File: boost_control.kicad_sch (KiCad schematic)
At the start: 0 parts

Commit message: Working on 5v supply
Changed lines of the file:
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@@
 	(generator_version "9.0")
 	(paper "A4")
-	(wire
-		(pts
-			(xy 116.84 91.44) (xy 133.35 91.44)
-		)
-		(stroke
-			(width 0)
-			(type default)
-		)
-	)
 	(bus
 		(pts
@@
 		)
 	)
-	(hierarchical_label "FB_OUT"
-		(shape output)
-		(at 133.35 91.44 0)
-		(effects
-			(font
-				(size 1.27 1.27)
-			)
-			(justify left)
-		)
-	)

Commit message: Adding control stuff
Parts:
- added C75: 100nF, Capacitor_SMD:C_0603_1608Metric, symbol Device:C
- added C78: 10uF, Capacitor_SMD:C_0805_2012Metric, symbol Device:C
- added R72: 15k, Resistor_SMD:R_0603_1608Metric, symbol Device:R_US
- added R74: 274k, Resistor_SMD:R_0603_1608Metric, symbol Device:R_US
- added U16: AD5259BRMZ100, RM_10_ADI, symbol _AD5259:AD5259BRMZ100
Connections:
- new net: R72.1, U16.1 (W), U16.10 (A)
- new net: R74.1, U16.9 (B)
- new net +3V3: U16.6 (VLOGIC)
- new net +5V: C75.1, C78.1, U16.8 (VDD)
- new net GND: C75.2, C78.2, U16.7 (GND)
- new net R+: R72.2
- new net R-: R74.2
- new net SCL: U16.5 (SCL)
- new net SDA: U16.4 (SDA)
- no-connect marks 0 -> 2

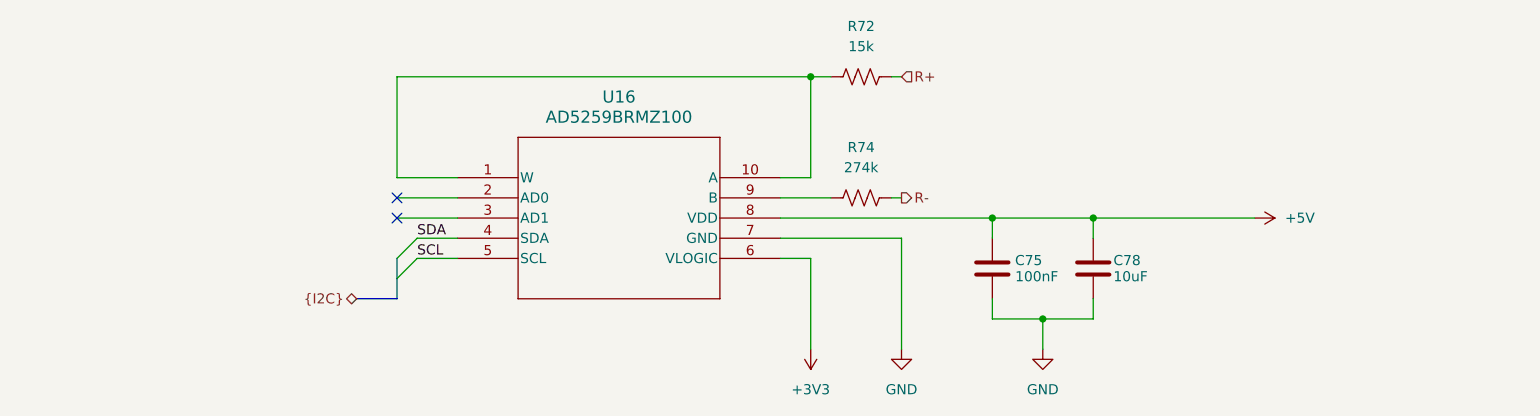
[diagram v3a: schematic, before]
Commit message: Adding in connections to schematic
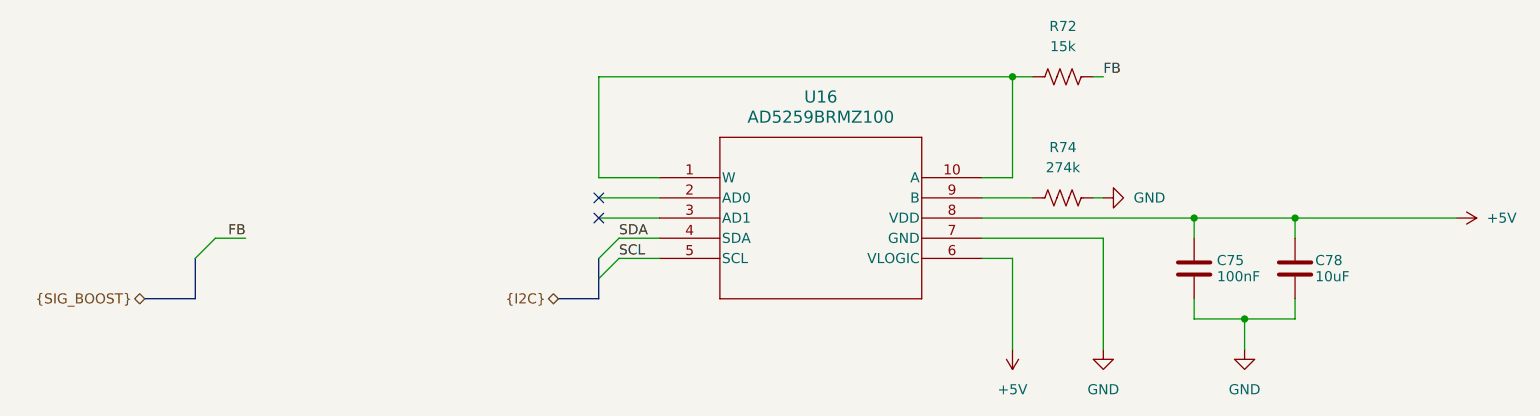
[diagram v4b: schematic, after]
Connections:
- net +3V3 is gone; now on net +5V: U16.6 (VLOGIC)
- net R- is gone; now on net GND: R74.2
- net R+ renamed FB
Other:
- moved on the sheet: C75, C78, R72, R74, U16

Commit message: Working on layout now
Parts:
- U2: renamed from U16; footprint RM_10_ADI -> _Power_Board:RM_10_ADI
- renumbered C75 to C17, C78 to C18, R72 to R4, R74 to R5
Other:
- company: (none) -> Solar Airplane
- title: (none) -> Boost Control
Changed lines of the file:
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@@
 	(generator_version "9.0")
 	(paper "A4")
+	(title_block
+		(title "Boost Control")
+		(rev "1")
+		(company "Solar Airplane")
+		(comment 1 "Engineer: Ezzat Suhaime")
+		(comment 2 "Reviewer 1:")
+		(comment 3 "Reviewer 2:")
+	)
 	(junction
 		(at 200.66 95.25)
@@
 		(dnp no)
 		(fields_autoplaced yes)
-		(property "Reference" "U16"
+		(property "Reference" "U2"
 			(at 153.67 80.01 0)
 			(effects
@@
 			)
 		)
-		(property "Footprint" "RM_10_ADI"
+		(property "Footprint" "_Power_Board:RM_10_ADI"
 			(at 133.35 90.17 0)
 			(effects
@@
 			(project ""
 				(path "/99785679-20de-4827-b4cc-bc3c187068c9/9564929a-642e-4163-88c2-45054b63a5ed/09b4163a-819e-413e-b808-030375832f4a"
-					(reference "U16")
+					(reference "U2")
 					(unit 1)
 				)
 				(path "/99785679-20de-4827-b4cc-bc3c187068c9/9564929a-642e-4163-88c2-45054b63a5ed/84126d6b-9224-455f-9cea-3582a8eebe20"
-					(reference "U17")
+					(reference "U8")
 					(unit 1)
 				)
@@
 		(on_board yes)
 		(dnp no)
-		(property "Reference" "C78"
+		(property "Reference" "C18"
 			(at 215.9 100.584 0)
 			(effects
@@
 			(project "PowerBoard"
 				(path "/99785679-20de-4827-b4cc-bc3c187068c9/9564929a-642e-4163-88c2-45054b63a5ed/09b4163a-819e-413e-b808-030375832f4a"
-					(reference "C78")
+					(reference "C18")
 					(unit 1)
 				)
 				(path "/99785679-20de-4827-b4cc-bc3c187068c9/9564929a-642e-4163-88c2-45054b63a5ed/84126d6b-9224-455f-9cea-3582a8eebe20"
-					(reference "C79")
+					(reference "C46")
 					(unit 1)
 				)
@@
 		(dnp no)
 		(fields_autoplaced yes)
-		(property "Reference" "#PWR0123"
+		(property "Reference" "#PWR018"
 			(at 189.23 118.11 0)
 			(effects
@@
 			(project ""
 				(path "/99785679-20de-4827-b4cc-bc3c187068c9/9564929a-642e-4163-88c2-45054b63a5ed/09b4163a-819e-413e-b808-030375832f4a"
-					(reference "#PWR0123")
+					(reference "#PWR018")
 					(unit 1)
 				)
 				(path "/99785679-20de-4827-b4cc-bc3c187068c9/9564929a-642e-4163-88c2-45054b63a5ed/84126d6b-9224-455f-9cea-3582a8eebe20"
-					(reference "#PWR0124")
+					(reference "#PWR058")
 					(unit 1)
 				)
@@
 		(dnp no)
 		(fields_autoplaced yes)
-		(property "Reference" "R74"
+		(property "Reference" "R5"
 			(at 184.15 86.36 90)
 			(effects
@@
 			(project ""
 				(path "/99785679-20de-4827-b4cc-bc3c187068c9/9564929a-642e-4163-88c2-45054b63a5ed/09b4163a-819e-413e-b808-030375832f4a"
-					(reference "R74")
+					(reference "R5")
 					(unit 1)
 				)
 				(path "/99785679-20de-4827-b4cc-bc3c187068c9/9564929a-642e-4163-88c2-45054b63a5ed/84126d6b-9224-455f-9cea-3582a8eebe20"
-					(reference "R75")
+					(reference "R25")
 					(unit 1)
 				)
@@
 		(dnp no)
 		(fields_autoplaced yes)
-		(property "Reference" "#PWR0127"
+		(property "Reference" "#PWR019"
 			(at 207.01 118.11 0)
 			(effects
@@
 			(project "PowerBoard"
 				(path "/99785679-20de-4827-b4cc-bc3c187068c9/9564929a-642e-4163-88c2-45054b63a5ed/09b4163a-819e-413e-b808-030375832f4a"
-					(reference "#PWR0127")
+					(reference "#PWR019")
 					(unit 1)
 				)
 				(path "/99785679-20de-4827-b4cc-bc3c187068c9/9564929a-642e-4163-88c2-45054b63a5ed/84126d6b-9224-455f-9cea-3582a8eebe20"
-					(reference "#PWR0128")
+					(reference "#PWR059")
 					(unit 1)
 				)
@@
 		(dnp no)
 		(fields_autoplaced yes)
-		(property "Reference" "R72"
+		(property "Reference" "R4"
 			(at 184.15 71.12 90)
 			(effects
@@
 			(project ""
 				(path "/99785679-20de-4827-b4cc-bc3c187068c9/9564929a-642e-4163-88c2-45054b63a5ed/09b4163a-819e-413e-b808-030375832f4a"
-					(reference "R72")
+					(reference "R4")
 					(unit 1)
 				)
 				(path "/99785679-20de-4827-b4cc-bc3c187068c9/9564929a-642e-4163-88c2-45054b63a5ed/84126d6b-9224-455f-9cea-3582a8eebe20"
-					(reference "R73")
+					(reference "R24")
 					(unit 1)
 				)
@@
 		(dnp no)
 		(fields_autoplaced yes)
-		(property "Reference" "#PWR0125"
+		(property "Reference" "#PWR020"
 			(at 229.87 95.25 0)
 			(effects
@@
 			(project ""
 				(path "/99785679-20de-4827-b4cc-bc3c187068c9/9564929a-642e-4163-88c2-45054b63a5ed/09b4163a-819e-413e-b808-030375832f4a"
-					(reference "#PWR0125")
+					(reference "#PWR020")
 					(unit 1)
 				)
 				(path "/99785679-20de-4827-b4cc-bc3c187068c9/9564929a-642e-4163-88c2-45054b63a5ed/84126d6b-9224-455f-9cea-3582a8eebe20"
-					(reference "#PWR0126")
+					(reference "#PWR060")
 					(unit 1)
 				)
@@
 		(dnp no)
 		(fields_autoplaced yes)
-		(property "Reference" "#PWR01"
+		(property "Reference" "#PWR016"
 			(at 177.8 107.95 0)
 			(effects
@@
 			(project ""
 				(path "/99785679-20de-4827-b4cc-bc3c187068c9/9564929a-642e-4163-88c2-45054b63a5ed/09b4163a-819e-413e-b808-030375832f4a"
-					(reference "#PWR01")
+					(reference "#PWR016")
 					(unit 1)
 				)
 				(path "/99785679-20de-4827-b4cc-bc3c187068c9/9564929a-642e-4163-88c2-45054b63a5ed/84126d6b-9224-455f-9cea-3582a8eebe20"
-					(reference "#PWR0129")
+					(reference "#PWR056")
 					(unit 1)
 				)
@@
 		(dnp no)
 		(fields_autoplaced yes)
-		(property "Reference" "#PWR0131"
+		(property "Reference" "#PWR017"
 			(at 195.58 92.71 0)
 			(effects
@@
 			(project ""
 				(path "/99785679-20de-4827-b4cc-bc3c187068c9/9564929a-642e-4163-88c2-45054b63a5ed/09b4163a-819e-413e-b808-030375832f4a"
-					(reference "#PWR0131")
+					(reference "#PWR017")
 					(unit 1)
 				)
 				(path "/99785679-20de-4827-b4cc-bc3c187068c9/9564929a-642e-4163-88c2-45054b63a5ed/84126d6b-9224-455f-9cea-3582a8eebe20"
-					(reference "#PWR0132")
+					(reference "#PWR057")
 					(unit 1)
 				)
@@
 		(on_board yes)
 		(dnp no)
-		(property "Reference" "C75"
+		(property "Reference" "C17"
 			(at 205.232 100.584 0)
 			(effects
@@
 			(project "PowerBoard"
 				(path "/99785679-20de-4827-b4cc-bc3c187068c9/9564929a-642e-4163-88c2-45054b63a5ed/09b4163a-819e-413e-b808-030375832f4a"
-					(reference "C75")
+					(reference "C17")
 					(unit 1)
 				)
 				(path "/99785679-20de-4827-b4cc-bc3c187068c9/9564929a-642e-4163-88c2-45054b63a5ed/84126d6b-9224-455f-9cea-3582a8eebe20"
-					(reference "C77")
-					(unit 1)
-				)
+					(reference "C45")
+					(unit 1)
+				)

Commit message: Cleaning up schematic
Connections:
- net FB: now also R5.2; no longer R4.2
- net GND: now also R4.2; no longer R5.2
- net at U2.1 (W), U2.10 (A): now also R5.1; no longer R4.1
- net at U2.9 (B): now also R4.1; no longer R5.1
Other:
- moved on the sheet: R4, R5
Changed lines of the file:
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@@
 	(symbol
 		(lib_id "Device:R_US")
-		(at 184.15 92.71 90)
+		(at 184.15 77.47 90)
 		(unit 1)
 		(exclude_from_sim no)
@@
 		(fields_autoplaced yes)
 		(property "Reference" "R5"
-			(at 184.15 86.36 90)
+			(at 184.15 71.12 90)
 			(effects
 				(font
@@
 		)
 		(property "Value" "274k"
-			(at 184.15 88.9 90)
+			(at 184.15 73.66 90)
 			(effects
 				(font
@@
 		)
 		(property "Footprint" "Resistor_SMD:R_0603_1608Metric"
-			(at 184.404 91.694 90)
+			(at 184.404 76.454 90)
 			(effects
 				(font
@@
 		)
 		(property "Datasheet" "https://industrial.panasonic.com/cdbs/www-data/pdf/RDM0000/AOA0000C307.pdf"
-			(at 184.15 92.71 0)
+			(at 184.15 77.47 0)
 			(effects
 				(font
@@
 		)
 		(property "Description" "RES SMD 274K OHM 0.1% 1/10W 0603"
-			(at 184.15 92.71 0)
+			(at 184.15 77.47 0)
 			(effects
 				(font
@@
 		)
 		(property "Mfr" "Panasonic Electronic Components"
-			(at 184.15 92.71 0)
+			(at 184.15 77.47 0)
 			(effects
 				(font
@@
 		)
 		(property "Mfr P/N" "ERA-3AEB2743V"
-			(at 184.15 92.71 0)
+			(at 184.15 77.47 0)
 			(effects
 				(font
@@
 		)
 		(property "Supplier_1" "Digikey"
-			(at 184.15 92.71 0)
+			(at 184.15 77.47 0)
 			(effects
 				(font
@@
 		)
 		(property "Supplier_1 P/N" "P274KDBTR-ND"
-			(at 184.15 92.71 0)
+			(at 184.15 77.47 0)
 			(effects
 				(font
@@
 		)
 		(property "Supplier_1 Unit Price" "0.10000"
-			(at 184.15 92.71 0)
+			(at 184.15 77.47 0)
 			(effects
 				(font
@@
 		)
 		(property "Supplier_1 Price @ Qty" "1"
-			(at 184.15 92.71 0)
+			(at 184.15 77.47 0)
 			(effects
 				(font
@@
 		)
 		(property "Supplier_2" ""
-			(at 184.15 92.71 0)
+			(at 184.15 77.47 0)
 			(effects
 				(font
@@
 		)
 		(property "Supplier_2 P/N" ""
-			(at 184.15 92.71 0)
+			(at 184.15 77.47 0)
 			(effects
 				(font
@@
 		)
 		(property "Supplier_2 Unit Price" ""
-			(at 184.15 92.71 0)
+			(at 184.15 77.47 0)
 			(effects
 				(font
@@
 		)
 		(property "Supplier_2 Price @ Qty" ""
-			(at 184.15 92.71 0)
+			(at 184.15 77.47 0)
 			(effects
 				(font
@@
 	(symbol
 		(lib_id "Device:R_US")
-		(at 184.15 77.47 90)
+		(at 184.15 92.71 90)
 		(unit 1)
 		(exclude_from_sim no)
@@
 		(fields_autoplaced yes)
 		(property "Reference" "R4"
-			(at 184.15 71.12 90)
+			(at 184.15 86.36 90)
 			(effects
 				(font
@@
 		)
 		(property "Value" "15k"
-			(at 184.15 73.66 90)
+			(at 184.15 88.9 90)
 			(effects
 				(font
@@
 		)
 		(property "Footprint" "Resistor_SMD:R_0603_1608Metric"
-			(at 184.404 76.454 90)
+			(at 184.404 91.694 90)
 			(effects
 				(font
@@
 		)
 		(property "Datasheet" "https://industrial.panasonic.com/cdbs/www-data/pdf/RDM0000/AOA0000C307.pdf"
-			(at 184.15 77.47 0)
+			(at 184.15 92.71 0)
 			(effects
 				(font
@@
 		)
 		(property "Description" "RES SMD 15K OHM 0.1% 1/10W 0603"
-			(at 184.15 77.47 0)
+			(at 184.15 92.71 0)
 			(effects
 				(font
@@
 		)
 		(property "Mfr" "Panasonic Electronic Components"
-			(at 184.15 77.47 0)
+			(at 184.15 92.71 0)
 			(effects
 				(font
@@
 		)
 		(property "Mfr P/N" "ERA-3AEB153V"
-			(at 184.15 77.47 0)
+			(at 184.15 92.71 0)
 			(effects
 				(font
@@
 		)
 		(property "Supplier_1" "Digikey"
-			(at 184.15 77.47 0)
+			(at 184.15 92.71 0)
 			(effects
 				(font
@@
 		)
 		(property "Supplier_1 P/N" "P15KDBTR-ND"
-			(at 184.15 77.47 0)
+			(at 184.15 92.71 0)
 			(effects
 				(font
@@
 		)
 		(property "Supplier_1 Unit Price" "0.10000"
-			(at 184.15 77.47 0)
+			(at 184.15 92.71 0)
 			(effects
 				(font
@@
 		)
 		(property "Supplier_1 Price @ Qty" "1"
-			(at 184.15 77.47 0)
+			(at 184.15 92.71 0)
 			(effects
 				(font
@@
 		)
 		(property "Supplier_2" ""
-			(at 184.15 77.47 0)
+			(at 184.15 92.71 0)
 			(effects
 				(font
@@
 		)
 		(property "Supplier_2 P/N" ""
-			(at 184.15 77.47 0)
+			(at 184.15 92.71 0)
 			(effects
 				(font
@@
 		)
 		(property "Supplier_2 Unit Price" ""
-			(at 184.15 77.47 0)
+			(at 184.15 92.71 0)
 			(effects
 				(font
@@
 		)
 		(property "Supplier_2 Price @ Qty" ""
-			(at 184.15 77.47 0)
-			(effects
-				(font
+			(at 184.15 92.71 0)
+			(effects
+				(font

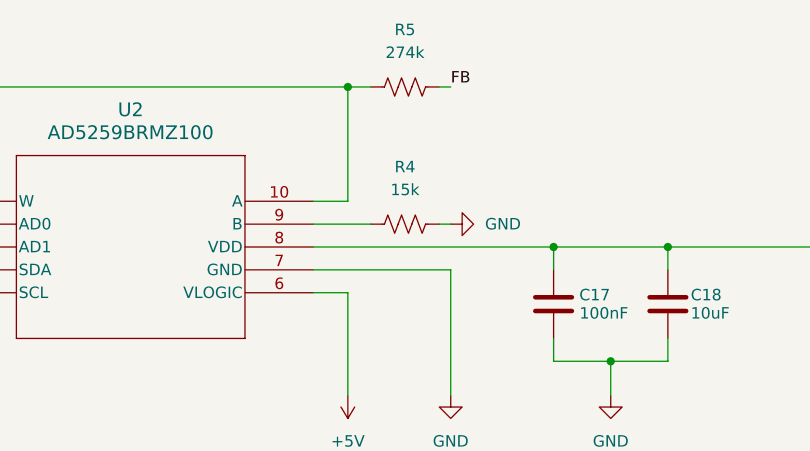
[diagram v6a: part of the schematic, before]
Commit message: Starting bus load switch layout
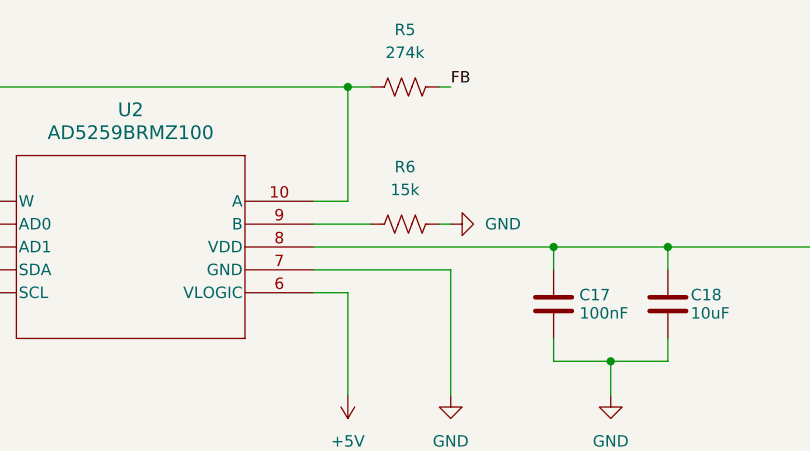
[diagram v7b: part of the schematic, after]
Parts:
- renumbered R4 to R6
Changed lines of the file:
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@@
 				)
 				(path "/99785679-20de-4827-b4cc-bc3c187068c9/9564929a-642e-4163-88c2-45054b63a5ed/84126d6b-9224-455f-9cea-3582a8eebe20"
-					(reference "U8")
+					(reference "U6")
 					(unit 1)
 				)
@@
 				)
 				(path "/99785679-20de-4827-b4cc-bc3c187068c9/9564929a-642e-4163-88c2-45054b63a5ed/84126d6b-9224-455f-9cea-3582a8eebe20"
-					(reference "C46")
+					(reference "C53")
 					(unit 1)
 				)
@@
 				)
 				(path "/99785679-20de-4827-b4cc-bc3c187068c9/9564929a-642e-4163-88c2-45054b63a5ed/84126d6b-9224-455f-9cea-3582a8eebe20"
-					(reference "#PWR058")
+					(reference "#PWR077")
 					(unit 1)
 				)
@@
 				)
 				(path "/99785679-20de-4827-b4cc-bc3c187068c9/9564929a-642e-4163-88c2-45054b63a5ed/84126d6b-9224-455f-9cea-3582a8eebe20"
-					(reference "R25")
+					(reference "R21")
 					(unit 1)
 				)
@@
 				)
 				(path "/99785679-20de-4827-b4cc-bc3c187068c9/9564929a-642e-4163-88c2-45054b63a5ed/84126d6b-9224-455f-9cea-3582a8eebe20"
-					(reference "#PWR059")
+					(reference "#PWR078")
 					(unit 1)
 				)
@@
 		(dnp no)
 		(fields_autoplaced yes)
-		(property "Reference" "R4"
+		(property "Reference" "R6"
 			(at 184.15 86.36 90)
 			(effects
@@
 			(project ""
 				(path "/99785679-20de-4827-b4cc-bc3c187068c9/9564929a-642e-4163-88c2-45054b63a5ed/09b4163a-819e-413e-b808-030375832f4a"
-					(reference "R4")
+					(reference "R6")
 					(unit 1)
 				)
 				(path "/99785679-20de-4827-b4cc-bc3c187068c9/9564929a-642e-4163-88c2-45054b63a5ed/84126d6b-9224-455f-9cea-3582a8eebe20"
-					(reference "R24")
+					(reference "R22")
 					(unit 1)
 				)
@@
 				)
 				(path "/99785679-20de-4827-b4cc-bc3c187068c9/9564929a-642e-4163-88c2-45054b63a5ed/84126d6b-9224-455f-9cea-3582a8eebe20"
-					(reference "#PWR060")
+					(reference "#PWR079")
 					(unit 1)
 				)
@@
 				)
 				(path "/99785679-20de-4827-b4cc-bc3c187068c9/9564929a-642e-4163-88c2-45054b63a5ed/84126d6b-9224-455f-9cea-3582a8eebe20"
-					(reference "#PWR056")
+					(reference "#PWR075")
 					(unit 1)
 				)
@@
 				)
 				(path "/99785679-20de-4827-b4cc-bc3c187068c9/9564929a-642e-4163-88c2-45054b63a5ed/84126d6b-9224-455f-9cea-3582a8eebe20"
-					(reference "#PWR057")
+					(reference "#PWR076")
 					(unit 1)
 				)
@@
 				)
 				(path "/99785679-20de-4827-b4cc-bc3c187068c9/9564929a-642e-4163-88c2-45054b63a5ed/84126d6b-9224-455f-9cea-3582a8eebe20"
-					(reference "C45")
-					(unit 1)
-				)
+					(reference "C52")
+					(unit 1)
+				)

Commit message: Doing placement for 5V 3V3 IMU
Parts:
- U2: footprint _Power_Board:RM_10_ADI -> _PowerBoard:RM_10_ADI-M; Supplier_2 (none) -> Analog Devices; Supplier_2 P/N (none) -> C141953; Supplier_2 Price @ Qty (none) -> 1; Supplier_2 Unit Price (none) -> 3.2689
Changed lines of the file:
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@@
 			)
 		)
-		(property "Footprint" "_Power_Board:RM_10_ADI"
+		(property "Footprint" "_PowerBoard:RM_10_ADI-M"
 			(at 133.35 90.17 0)
 			(effects
@@
 			)
 		)
-		(property "Supplier_2" ""
+		(property "Supplier_2" "Analog Devices"
 			(at 133.35 90.17 0)
 			(effects
@@
 			)
 		)
-		(property "Supplier_2 P/N" ""
+		(property "Supplier_2 P/N" "C141953"
 			(at 133.35 90.17 0)
 			(effects
@@
 			)
 		)
-		(property "Supplier_2 Unit Price" ""
+		(property "Supplier_2 Unit Price" "3.2689"
 			(at 133.35 90.17 0)
 			(effects
@@
 			)
 		)
-		(property "Supplier_2 Price @ Qty" ""
+		(property "Supplier_2 Price @ Qty" "1"
 			(at 133.35 90.17 0)
 			(effects
